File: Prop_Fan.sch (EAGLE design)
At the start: 77 parts, among them J1 500075-1517, SW1 EVQ-Q2203W, U1 P8X32A, U10 MAX31855KASA+, U2 FT230X, U3 LM22678TJ-5.0/NOPB, U6 ADP3338AKCZ-3.3-RL, U8 CAT24C512WI-GT3, U9 MAX31855KASA+, X1 ABLS3-6.000MHZ-D4Y-T

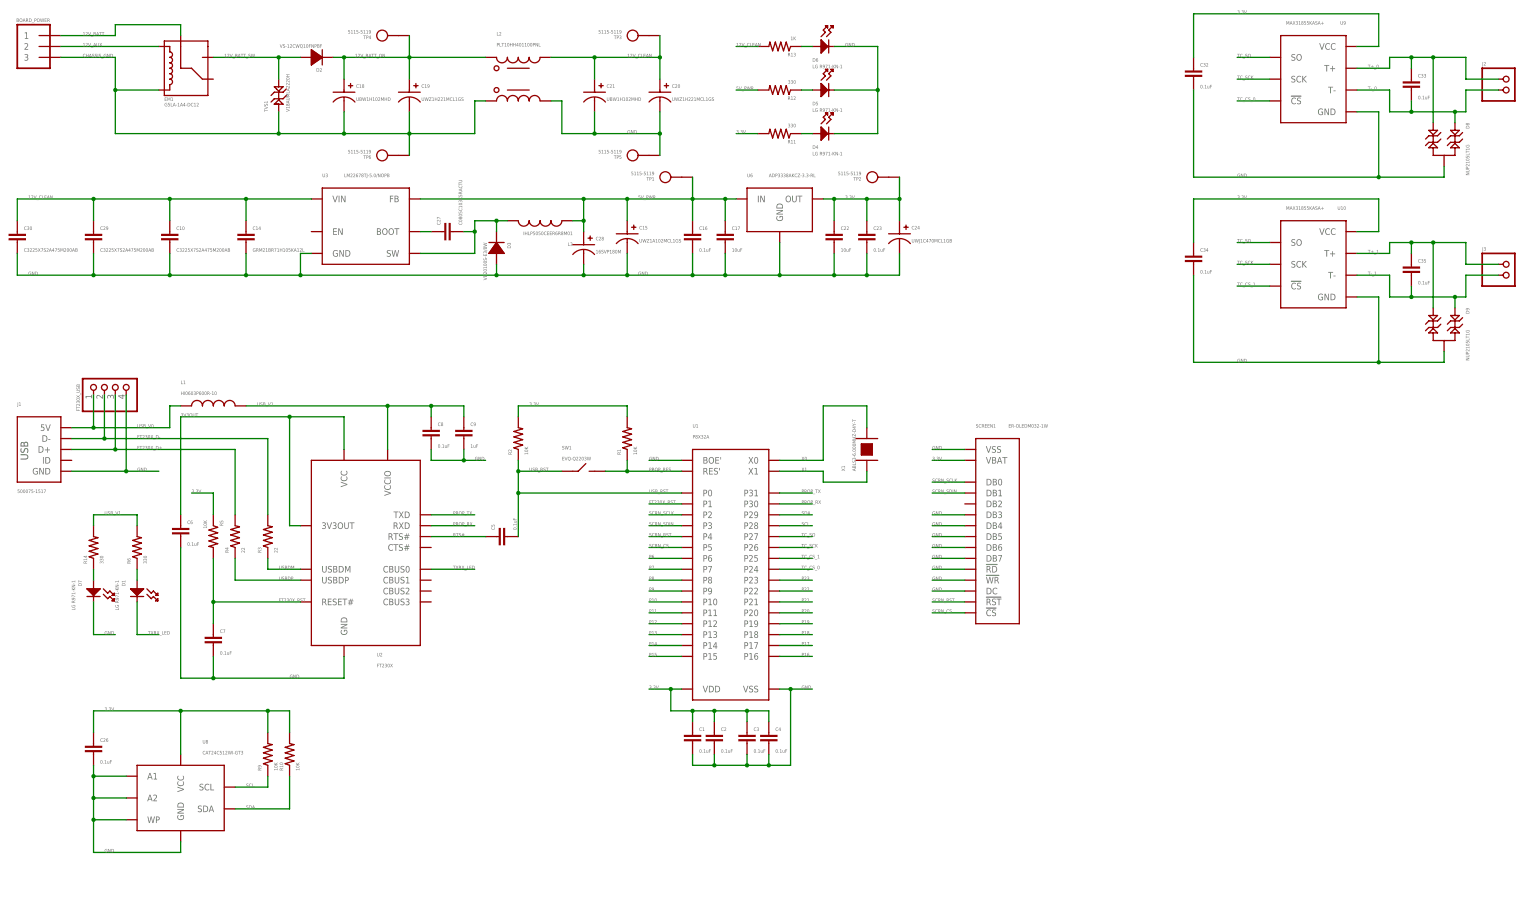
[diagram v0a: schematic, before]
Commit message: Need to add outputs.
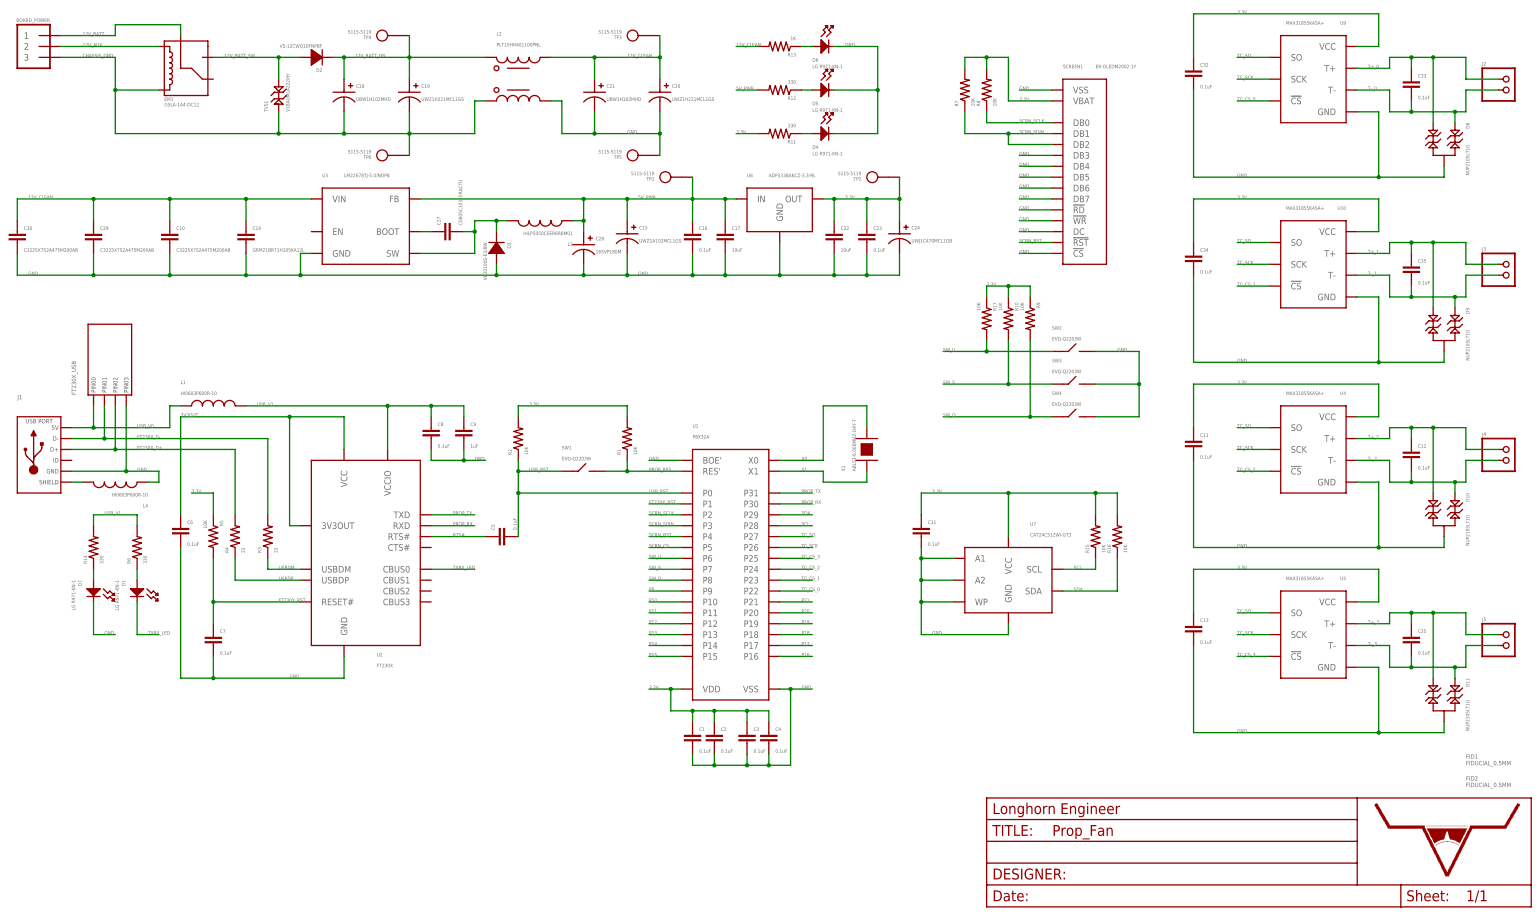
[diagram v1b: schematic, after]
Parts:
- removed C26: 0.1uF, PP_Passives:CAPACITOR_NON_POLAR0805
- removed U8: CAT24C512WI-GT3, PP_DigitalIC:CAT24M01XI-T2SOIC-8_W
- added C11, C12, C13, C25, C31: 0.1uF, PP_Passives:CAPACITOR_NON_POLAR0805
- added D10, D11: NUP2105LT1G, PP_Passives:TVS_DIODE_DUALSOT-23
- added FID1, FID2: FIDUCIAL_0.5MM, MF_Aesthetics:FIDUCIAL_0.5MM
- added J4, J5: (no value), PP_Connectors:PH_1X02SCREW_TERM
- added L4: HI0603P600R-10, PP_Passives:INDUCTOR0603
- added R15, R16, R17, R7, R8: 10K, PP_Passives:RESISTOR0805
- added SW2, SW3, SW4: EVQ-Q2203W, PP_Electromechanical:SPSTEVQ-Q2203W
- added U$1: LHE_FRAME, PP_Aesthetics:LHE_FRAME
- added U4, U5: MAX31855KASA+, PP_Sensors:MAX31855SO-8
- added U7: CAT24C512WI-GT3, PP_DigitalIC:CAT24M01XI-T2SOIC-8_W
- J1: value 500075-1517 -> (none); device PP_Connectors:USB500075-1517 -> MF_Connectors:USB_MICRO_RIGHT
- SCREEN1: value ER-OLEDM032-1W -> ER-OLEDM2002-1Y; device PP_Displays:ER-OLEDM032ER-OLEDM032 -> PP_Displays:ER-OLEDM032ER-OLEDM2002_PTH
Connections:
- removed net P22: U1.P22
- removed net P23: U1.P23
- removed net P6: U1.P6
- removed net P7: U1.P7
- removed net P8: U1.P8
- new net N$3: J1.SLD, L4.P$2
- new net SW_D: R9.2, SW4.A, U1.P8
- new net SW_S: R10.2, SW3.A, U1.P7
- new net SW_U: R17.2, SW2.A, U1.P6
- new net T+_2: C12.1, D10.2, J4.1, U4.T+
- new net T+_3: C25.1, D11.2, J5.1, U5.T+
- new net T-_2: C12.2, D10.1, J4.2, U4.T-
- new net T-_3: C25.2, D11.1, J5.2, U5.T-
- new net TC_CS_2: U1.P24, U4.!CS
- new net TC_CS_3: U1.P25, U5.!CS
- net 3.3V: now also C11.1, C13.1, C31.1, R10.1, R15.2, R16.2, R17.1, R7.2, R8.2, R9.1, U4.VCC, U5.VCC, U7.VCC; no longer C26.1, R10.2, R9.2, U8.VCC
- net GND: now also C11.2, C13.2, C31.2, D10.3, D11.3, L4.P$1, SCREEN1.!CS, SW2.B, SW3.B, SW4.B, U4.GND, U5.GND, U7.A1, U7.A2, U7.GND, U7.WP; no longer C26.2, U8.A1, U8.A2, U8.GND, U8.WP
- net SCL: now also R15.1, U7.SCL; no longer R9.1, U8.SCL
- net SCRN_CS: no longer SCREEN1.!CS
- net SCRN_SCLK: now also R8.1
- net SCRN_SDIN: now also R7.1, SCREEN1.DB2
- net SDA: now also R16.1, U7.SDA; no longer R10.1, U8.SDA
- net TC_CS_0: now also U1.P22; no longer U1.P24
- net TC_CS_1: now also U1.P23; no longer U1.P25
- net TC_SCK: now also U4.SCK, U5.SCK
- net TC_SO: now also U4.SO, U5.SO
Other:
- moved on the sheet: R10, R9, SCREEN1

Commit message: Starting Layout.
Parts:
- removed D7: LG R971-KN-1, PP_LED:LED_SINGLE0805
- removed FT230X_USB: (no value), PP_Connectors:PH_1X04HEADER_PTH
- removed R14: 330, PP_Passives:RESISTOR0805
- added R18: 0, PP_Passives:RESISTOR0805
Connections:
- removed net N$4: D7.ANODE, R14.1
- net 5V_PWR: now also R18.1
- net FT230X_D+: no longer FT230X_USB.3
- net FT230X_D-: no longer FT230X_USB.2
- net GND: no longer D7.CATHODE, FT230X_USB.4
- net USB_V0: no longer FT230X_USB.1
- net USB_V1: now also R18.2; no longer R14.2

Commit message: Working on power layout.
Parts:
- SCREEN1: device PP_Displays:ER-OLEDM032ER-OLEDM2002_PTH -> PP_Displays:ER-OLEDM032ER-OLEDM032_PTH
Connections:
- removed net P9: U1.P9
- net GND: no longer SCREEN1.!CS
- net SCRN_CS: now also SCREEN1.!CS, U1.P6
- net SCRN_SDIN: no longer SCREEN1.DB2
- net SW_D: now also U1.P9; no longer U1.P8
- net SW_S: now also U1.P8; no longer U1.P7
- net SW_U: now also U1.P7; no longer U1.P6

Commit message: Need to add optos.
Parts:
- removed EM1: G5LA-1A4-DC12, PP_Electromechanical:SPDT_RELAYG5LA
- removed L4: HI0603P600R-10, PP_Passives:INDUCTOR0603
- removed R18: 0, PP_Passives:RESISTOR0805
- removed SCREEN1: ER-OLEDM2002-1Y, PP_Displays:ER-OLEDM032ER-OLEDM032_PTH
- added C26, C38, C39, C40, C41: 0.1uF, PP_Passives:CAPACITOR_NON_POLAR_0805
- added C36: UWJ1C470MCL1GB, PP_Passives:CAPACITOR_POLARIZED_6.3MM_SMD
- added C37: 47pF, PP_Passives:CAPACITOR_NON_POLAR_0805
- added D12, D7: NUP2105LT1G, PP_Passives:TVS_DIODE_DUALSOT-23
- added J6, J7: (no value), PP_Connectors:PH_1X02SCREW_TERM
- added LCD1: ER-OLEDM2002-1, PP_Displays:ER-OLEDM2002-1
- added R14: 10K, PP_Passives:RESISTOR_0805
- added U11, U12: MAX31855KASA+, PP_Sensors:MAX31855
- added U8: IP4234CZ6, PP_Passives:IP4234CZ6
- C1, C11, C12, C13, C14, C16, C17, C2, C22, C23, C25, C27, C3, C31, C32, C33, C34, C35, C4, C5, C7, C8, C9: device PP_Passives:CAPACITOR_NON_POLAR0805 -> PP_Passives:CAPACITOR_NON_POLAR_0805
- C10, C29, C30: device PP_Passives:CAPACITOR_NON_POLAR1210 -> PP_Passives:CAPACITOR_NON_POLAR_1210
- C15, C19, C20: device PP_Passives:CAPACITOR_POLARIZED10MM_SMD -> PP_Passives:CAPACITOR_POLARIZED_10MM_SMD
- C18, C21: device PP_Passives:CAPACITOR_POLARIZED12.5MM_PTH -> PP_Passives:CAPACITOR_POLARIZED_12.5MM_PTH
- C24: device PP_Passives:CAPACITOR_POLARIZED6.3MM_SMD -> PP_Passives:CAPACITOR_POLARIZED_6.3MM_SMD
- C28: device PP_Passives:CAPACITOR_POLARIZED8MM_SMD -> PP_Passives:CAPACITOR_POLARIZED_8MM_SMD
- C6: value 0.1uF -> 47pF; device PP_Passives:CAPACITOR_NON_POLAR0805 -> PP_Passives:CAPACITOR_NON_POLAR_0805
- D1, D4, D5, D6: device PP_LED:LED_SINGLE0805 -> PP_LED:LED_SINGLE_0805
- D2: device PP_Passives:DIODED-PAK(TO-252AA) -> PP_Passives:DIODE_D-PAK(TO-252AA)
- D3: device PP_Passives:DIODED2PAK(TO-263AB) -> PP_Passives:DIODE_D2PAK(TO-263AB)
- L1: value HI0603P600R-10 -> MI0603K300R-10; device PP_Passives:INDUCTOR0603 -> PP_Passives:INDUCTOR_0603
- L2: device PP_Passives:COMMON_MODE_INDUCTORPLT10H -> PP_Passives:COMMON_MODE_INDUCTOR_PLT10H
- L3: device PP_Passives:INDUCTORIHLP-5050 -> PP_Passives:INDUCTOR_IHLP-5050
- R1, R10, R11, R13, R15, R16, R17, R2, R6, R7, R8, R9: device PP_Passives:RESISTOR0805 -> PP_Passives:RESISTOR_0805
- R12: value 330 -> 390; device PP_Passives:RESISTOR0805 -> PP_Passives:RESISTOR_0805
- R3, R4: value 22 -> 27; device PP_Passives:RESISTOR0805 -> PP_Passives:RESISTOR_0805
- R5: value 10K -> 4.7K; device PP_Passives:RESISTOR0805 -> PP_Passives:RESISTOR_0805
- SW1, SW2, SW3, SW4: device PP_Electromechanical:SPSTEVQ-Q2203W -> PP_Electromechanical:SPST_EVQ-Q2203W
- TP1, TP2, TP3, TP4, TP5, TP6: device PP_Connectors:TEST_POINT_SINGLEKEYSTONE_5115-5119 -> PP_Connectors:TEST_POINT_SINGLE_KEYSTONE_5115-5119
- TVS1: device PP_Passives:TVS_DIODE2220 -> PP_Passives:TVS_DIODE_2220
- U1: value P8X32A -> P8X32A-Q44; device PP_DigitalIC:P8X32A_PROPELLERLQFP-44 -> MF_IC_Digital:P8X32A-Q44
- U10, U4, U5, U9: device PP_Sensors:MAX31855SO-8 -> PP_Sensors:MAX31855
- U2: value FT230X -> FT230XS; device PP_DigitalIC:FT230XSSOP-16 -> PP_DigitalIC:FT230XQ
- U7: device PP_DigitalIC:CAT24M01XI-T2SOIC-8_W -> PP_DigitalIC:EEPROM_I2CSOIC-8_W
- X1: value ABLS3-6.000MHZ-D4Y-T -> ABMM-6.000MHZ-B2-T; device PP_FreqCtrl:CRYSTALHC-49 -> MF_Frequency_Control:XTL_7MMX5MM
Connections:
- net RTS# renamed !RTS
- removed net 12V_AUX: BOARD_POWER.2, EM1.2
- removed net 12V_BATT_SW: D2.ANODE, EM1.3, TVS1.P$2
- removed net FT230X_RST: C7.1, R5.2, U1.P1, U2.RESET#
- removed net P20: U1.P20
- removed net P21: U1.P21
- removed net SCRN_CS: SCREEN1.!CS, U1.P5, U1.P6
- removed net SCRN_SCLK: R8.1, SCREEN1.DB0, U1.P2
- removed net SCRN_SDIN: R7.1, SCREEN1.DB1, U1.P3
- removed net USB_V1: C8.1, C9.1, L1.P$2, R18.2, R6.2, U2.VCCIO
- new net N$10: C6.1, R4.2, U8.I/O1B
- new net N$6: C37.1, R3.2, U8.I/O2B
- new net P1: U1.P1
- new net P5: U1.P5
- new net P6: U1.P6
- new net SCRN_SCL: LCD1.D0, R8.1, U1.P2
- new net SCRN_SDA: LCD1.D1, LCD1.D2, R7.1, U1.P3
- new net TC_CS_4: U1.P24, U5.!CS
- new net TC_CS_5: U1.P25, U12.!CS
- new net VBUS_S: R14.1, R5.1, U2.CBUS3
- net 12V_BATT: now also D2.ANODE, TVS1.P$2; no longer EM1.1
- net 3.3V: now also C26.1, C36.POS, C38.1, C40.1, C8.1, C9.1, LCD1.VDD, R6.2, U11.VCC, U12.VCC, U2.VCC; no longer R5.1, SCREEN1.VBAT
- net 3V3OUT: now also C7.1, U2.RESET#, U2.VCCIO; no longer C6.1, U2.VCC
- net 5V_PWR: no longer R18.1
- net CHASSIS_GND: no longer EM1.5
- net FT230X_D+: now also U8.I/O1A; no longer R4.2
- net FT230X_D-: now also U8.I/O2A; no longer R3.2
- net GND: now also C26.2, C36.NEG, C37.2, C38.2, C40.2, D12.3, D7.3, L1.P$1, LCD1.CS, LCD1.D3, LCD1.D4, LCD1.D5, LCD1.D6, LCD1.D7, LCD1.DC, LCD1.RD, LCD1.RW, LCD1.VSS, R14.2, U11.GND, U12.GND, U8.GND, X1.GND; no longer L4.P$1, SCREEN1.!RD, SCREEN1.!WR, SCREEN1.DB3, SCREEN1.DB4, SCREEN1.DB5, SCREEN1.DB6, SCREEN1.DB7, SCREEN1.DC, SCREEN1.VSS
- net N$3: now also L1.P$2; no longer L4.P$2
- net SCRN_RST: now also LCD1.RSE; no longer SCREEN1.!RST
- net T+_1: now also C39.1, D7.2, J6.1, U11.T+
- net T+_3: now also C41.1, D12.2, J7.1, U12.T+
- net T-_1: now also C39.2, D7.1, J6.2, U11.T-
- net T-_3: now also C41.2, D12.1, J7.2, U12.T-
- net TC_CS_0: now also U1.P20; no longer U1.P22
- net TC_CS_1: now also U1.P21; no longer U1.P23
- net TC_CS_2: now also U1.P22, U11.!CS; no longer U1.P24, U4.!CS
- net TC_CS_3: now also U1.P23, U4.!CS; no longer U1.P25, U5.!CS
- net TC_SCK: now also U11.SCK, U12.SCK
- net TC_SO: now also U11.SO, U12.SO
- net USB_V0: now also R5.2, U8.VB; no longer L1.P$1
- net X0: now also X1.X0; no longer X1.P$2
- net X1: now also X1.X1; no longer X1.P$1
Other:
- moved on the sheet: BOARD_POWER, C1, C10, C11, C12, C13, C14, C16, C17, C2, C22, C23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

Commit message: Working on Schematic. Need to add optos. Display Added.
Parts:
- removed BOARD_POWER: (no value), PP_Connectors:PH_1X03HEADER_PTH
- removed C13, C25, C26, C40, C41, C7, C8: 0.1uF, PP_Passives:CAPACITOR_NON_POLAR_0805
- removed C36: UWJ1C470MCL1GB, PP_Passives:CAPACITOR_POLARIZED_6.3MM_SMD
- removed C37: 47pF, PP_Passives:CAPACITOR_NON_POLAR_0805
- removed C9: 1uF, PP_Passives:CAPACITOR_NON_POLAR_0805
- removed D1: LG R971-KN-1, PP_LED:LED_SINGLE_0805
- removed D11, D12: NUP2105LT1G, PP_Passives:TVS_DIODE_DUALSOT-23
- removed J5, J6, J7: (no value), PP_Connectors:PH_1X02SCREW_TERM
- removed L1: MI0603K300R-10, PP_Passives:INDUCTOR_0603
- removed LCD1: ER-OLEDM2002-1, PP_Displays:ER-OLEDM2002-1
- removed SW1: EVQ-Q2203W, PP_Electromechanical:SPST_EVQ-Q2203W
- removed U12: MAX31855KASA+, PP_Sensors:MAX31855
- removed U2: FT230XS, PP_DigitalIC:FT230XQ
- removed U3: LM22678TJ-5.0/NOPB, PP_PowerIC:LM22679TO-263-7_TI
- removed U8: IP4234CZ6, PP_Passives:IP4234CZ6
- added BOARD_PWR: (no value), PP_Connectors:CON_01X03_640454-3
- added DISP1: 61201621621, PP_Displays:CU40056-UW1J
- added PROP_TC: TC2030-FTDI-TTL-232R, PP_Connectors:CON_02X03_TC2030
- added PROP_UART: (no value), PP_Connectors:CON_01X06_2.54MM_PIN_HEADER
- added R18: 120, PP_Passives:RESISTOR_0805
- C6: value 47pF -> 10uF
- D4, D5, D6: value LG R971-KN-1 -> MF-LED-0805-RED
- J1: value (none) -> 1546215-2; device MF_Connectors:USB_MICRO_RIGHT -> PP_Connectors:CON_01X02_1546215-2; LABEL01 (none) -> T+; LABEL02 (none) -> T-
- J2, J3, J4: value (none) -> 1546215-2; device PP_Connectors:PH_1X02SCREW_TERM -> PP_Connectors:CON_01X02_1546215-2; LABEL01 (none) -> T+; LABEL02 (none) -> T-
- R14, R7, R8: value 10K -> 120
- R3, R4: value 27 -> 120
- R5: value 4.7K -> 120
- R6: value 330 -> 120
- U5: value MAX31855KASA+ -> LM22678TJ-5.0/NOPB; device PP_Sensors:MAX31855 -> PP_PowerIC:LM22678
- U6: device PP_PowerIC:FIXED_VOLTAGE_REGSOT-223_ALT -> PP_PowerIC:LINEAR_VOTLAGE_REGULATORS_ADP3338
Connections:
- removed net !RTS: C5.1, U2.RTS#
- removed net 3V3OUT: C7.1, U2.3V3OUT, U2.RESET#, U2.VCCIO
- removed net FT230X_D+: J1.D+, U8.I/O1A
- removed net FT230X_D-: J1.D-, U8.I/O2A
- removed net N$1: D1.ANODE, R6.1
- removed net N$10: C6.1, R4.2, U8.I/O1B
- removed net N$3: J1.SLD, L1.P$2
- removed net N$6: C37.1, R3.2, U8.I/O2B
- removed net P1: U1.P1
- removed net P10: U1.P10
- removed net P5: U1.P5
- removed net P6: U1.P6
- removed net PROP_RX: U1.P30, U2.RXD
- removed net PROP_TX: U1.P31, U2.TXD
- removed net SCRN_RST: LCD1.RSE, U1.P4
- removed net SCRN_SCL: LCD1.D0, R8.1, U1.P2
- removed net SCRN_SDA: LCD1.D1, LCD1.D2, R7.1, U1.P3
- removed net T+_3: C25.1, C41.1, D11.2, D12.2, J5.1, J7.1, U12.T+, U5.T+
- removed net T-_3: C25.2, C41.2, D11.1, D12.1, J5.2, J7.2, U12.T-, U5.T-
- removed net TC_CS_4: U1.P24, U5.!CS
- removed net TC_CS_5: U1.P25, U12.!CS
- removed net TXRX_LED: D1.CATHODE, U2.CBUS0
- removed net USBDM: R3.1, U2.USBDM
- removed net USBDP: R4.1, U2.USBDP
- removed net USB_RST: C5.2, R2.1, SW1.A, U1.P0
- removed net USB_V0: J1.5V, R5.2, U8.VB
- removed net VBUS_S: R14.1, R5.1, U2.CBUS3
- new net !RES!_PROP: C5.1, PROP_TC.PIN6, PROP_UART.6
- new net D4: DISP1.D4, R6.2
- new net D5: DISP1.D5, R5.2
- new net D6: DISP1.D6, R4.2
- new net D7: DISP1.D7, R3.2
- new net E1: DISP1.E1, R8.2
- new net E2: DISP1.E2, R7.2
- new net P20: U1.P20
- new net P21: U1.P21
- new net PROP_D4: R6.1, U1.P7
- new net PROP_D5: R5.1, U1.P8
- new net PROP_D6: R4.1, U1.P9
- new net PROP_D7: R3.1, U1.P10
- new net PROP_E1: R8.1, U1.P5
- new net PROP_E2: R7.1, U1.P6
- new net PROP_R/W: R14.1, U1.P4
- new net PROP_RS: R18.1, U1.P3
- new net R/W: DISP1.R/W, R14.2
- new net RS: DISP1.RS, R18.2
- new net RX_PROP: PROP_TC.PIN4, PROP_UART.4, U1.P31
- new net TX_PROP: PROP_TC.PIN3, PROP_UART.5, U1.P30
- net 12V_BATT: now also BOARD_PWR.PIN1; no longer BOARD_POWER.1
- net 12V_CLEAN: now also U5.VIN; no longer U3.VIN
- net 3.3V: no longer C13.1, C26.1, C36.POS, C40.1, C8.1, C9.1, LCD1.VDD, R6.2, R7.2, R8.2, U12.VCC, U2.VCC, U5.VCC
- net 5V_PWR: now also C6.1, DISP1.VCC, U5.FB; no longer U3.FB
- net CHASSIS_GND: now also BOARD_PWR.PIN3; no longer BOARD_POWER.3
- net GND: now also DISP1.D0, DISP1.D1, DISP1.D2, DISP1.D3, DISP1.GND, PROP_TC.PIN5, PROP_UART.1; no longer C13.2, C26.2, C36.NEG, C37.2, C40.2, C7.2, C8.2, C9.2, D11.3, D12.3, J1.GND, L1.P$1, LCD1.CS, LCD1.D3, LCD1.D4, LCD1.D5, LCD1.D6, LCD1.D7, LCD1.DC, LCD1.RD, LCD1.RW, LCD1.VSS, R14.2, U12.GND, U2.GND, U3.GND, U8.GND
- net N$2: now also U5.BOOT; no longer U3.BOOT
- net N$5: now also U5.SW; no longer U3.SW
- net PROP_RES: now also C5.2, R2.1; no longer SW1.B
- net SW_D: now also U1.P2; no longer U1.P9
- net SW_S: now also U1.P1; no longer U1.P8
- net SW_U: now also U1.P0; no longer U1.P7
- net T+_0: now also J1.PIN1; no longer J2.1
- net T+_1: now also J2.PIN1, J3.PIN1; no longer J3.1, J6.1
- net T+_2: now also J4.PIN1; no longer J4.1
- net T-_0: now also J1.PIN2; no longer J2.2
- net T-_1: now also J2.PIN2, J3.PIN2; no longer J3.2, J6.2
- net T-_2: now also J4.PIN2; no longer J4.2
- net TC_CS_0: now also U1.P22; no longer U1.P20
- net TC_CS_1: now also U1.P23; no longer U1.P21
- net TC_CS_2: now also U1.P24; no longer U1.P22
- net TC_CS_3: now also U1.P25; no longer U1.P23
- net TC_SCK: no longer U12.SCK, U5.SCK
- net TC_SO: no longer U12.SO, U5.SO
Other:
- moved on the sheet: C1, C10, C11, C12, C14, C15, C16, C17, C18, C19, C2, C20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

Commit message: Relay Control Hardware Complete.
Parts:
- added C7, C9: 0.1uF, PP_Passives:CAPACITOR_NON_POLAR_0805
- added R19, R20, R21, R22, R23, R24, R25, R26: 220, MF_Passives:RESISTOR_0603
- added R29, R30, R47, R48, R49, R50, R51, R52: 10K, MF_Passives:RESISTOR_0603
- added RELAYS, RELAYS1: 1-282834-0, PP_Connectors:CON_01X10_1-282834-0
- added U12, U13, U17, U18, U19, U2, U3, U8: MF-DSC-SOT233-BSS138, MF_Discrete_Semiconductor:N-CHANNEL_FET_SOT-23-3
- added U14: CD74HC595M96, PP_DigitalIC:CD74HC595M96
- added U16: CD74HC165M96, PP_DigitalIC:CD74HC165M96
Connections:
- removed net P11: U1.P11
- removed net P12: U1.P12
- removed net P13: U1.P13
- removed net P14: U1.P14
- removed net P15: U1.P15
- removed net P16: U1.P16
- new net 165_CLK: U1.P14, U16.CLK
- new net 165_DATA: U1.P15, U16.QH
- new net 165_LOAD: U1.P16, U16.LAT
- new net 595_CLK: U1.P11, U14.SHCP
- new net 595_DATA: U1.P12, U14.DS
- new net 595_LAT: U1.P13, U14.STCP
- new net IN_OPTO_1: U16.D1
- new net IN_OPTO_2: U16.D2
- new net IN_OPTO_3: U16.D3
- new net IN_OPTO_4: U16.D4
- new net IN_OPTO_5: U16.D5
- new net IN_OPTO_6: U16.D6
- new net IN_OPTO_7: U16.D7
- new net N$11: R19.P$2, R29.P$2, U2.GATE
- new net N$12: R20.P$2, R30.P$2, U3.GATE
- new net N$13: R21.P$2, R47.P$2, U8.GATE
- new net N$14: R22.P$2, R48.P$2, U12.GATE
- new net N$15: R23.P$2, R49.P$2, U13.GATE
- new net N$16: R24.P$2, R50.P$2, U17.GATE
- new net N$17: R25.P$2, R51.P$2, U18.GATE
- new net N$18: R26.P$2, R52.P$2, U19.GATE
- new net OUT_OPTO_0: R19.P$1, U14.Q0
- new net OUT_OPTO_1: R20.P$1, U14.Q1
- new net OUT_OPTO_2: R21.P$1, U14.Q2
- new net OUT_OPTO_3: R22.P$1, U14.Q3
- new net OUT_OPTO_4: R23.P$1, U14.Q4
- new net OUT_OPTO_5: R24.P$1, U14.Q5
- new net OUT_OPTO_6: R25.P$1, U14.Q6
- new net OUT_OPTO_7: R26.P$1, U14.Q7
- new net P$1: R29.P$1, R30.P$1, R47.P$1, R48.P$1, R49.P$1, R50.P$1, R51.P$1, R52.P$1, U12.SOURCE, U13.SOURCE, U17.SOURCE, U18.SOURCE, U19.SOURCE, U2.SOURCE, U3.SOURCE, U8.SOURCE
- new net RLY_0: RELAYS.1, U2.DRAIN
- new net RLY_1: RELAYS.2, U3.DRAIN
- new net RLY_2: RELAYS.3, U8.DRAIN
- new net RLY_3: RELAYS.4, U12.DRAIN
- new net RLY_4: RELAYS.5, U13.DRAIN
- new net RLY_5: RELAYS.6, U17.DRAIN
- new net RLY_6: RELAYS.7, U18.DRAIN
- new net RLY_7: RELAYS.8, U19.DRAIN
- net 3.3V: now also C7.1, C9.1, U14.MR, U14.VCC, U16.VCC
- net GND: now also C7.2, C9.2, U14.GND, U14.OE, U16.C_INH, U16.GND
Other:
- moved on the sheet: C11, C12, C33, C34, C35, C38, C39, C6, D10, D7, D8, D9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
